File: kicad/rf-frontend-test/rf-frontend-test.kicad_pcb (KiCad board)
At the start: 2 copper layers, 15 x 26.4 mm, 26 parts, among them J1 GPIO, J2 SPI, J3 PWR, U1 Si4463, Y1 30MHz

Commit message: clean sch2
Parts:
- U1: footprint Package_DFN_QFN:QFN-20-1EP_4x4mm_P0.5mm_EP2.6x2.6mm_ThermalVias -> Package_DFN_QFN:QFN-20-1EP_4x4mm_P0.5mm_EP2.6x2.6mm
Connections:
- U1 pad 5: unconnected-(U1-NC-Pad5) -> GND
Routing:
- net GND: track 5.49 -> 13.1 mm, vias 75 -> 159
- net ~{RF_EN}: track 11.6 -> 12.5 mm
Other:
- board size 15 x 26.4 mm -> 15 x 26.5 mm

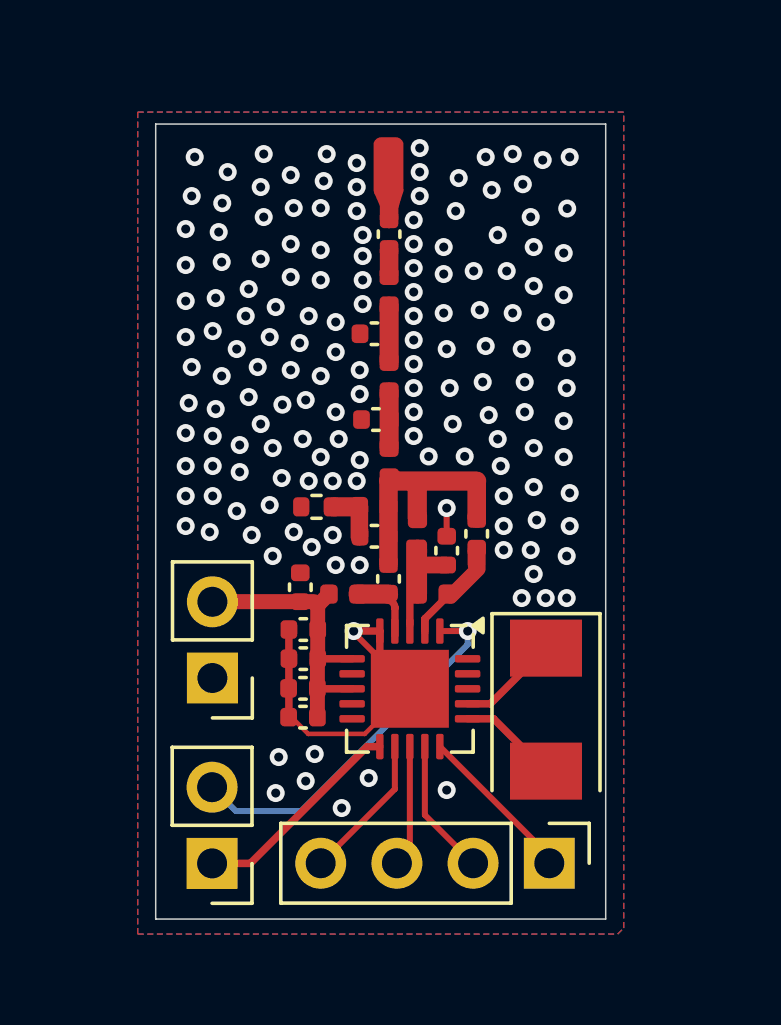
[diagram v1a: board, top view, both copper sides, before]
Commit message: Si4463 Transceiver Circuit V2.
Updated the transceiver board to make it compliant with EPL fab limitations. Fixed all GND vias, added Header Pins for the GPIO pins
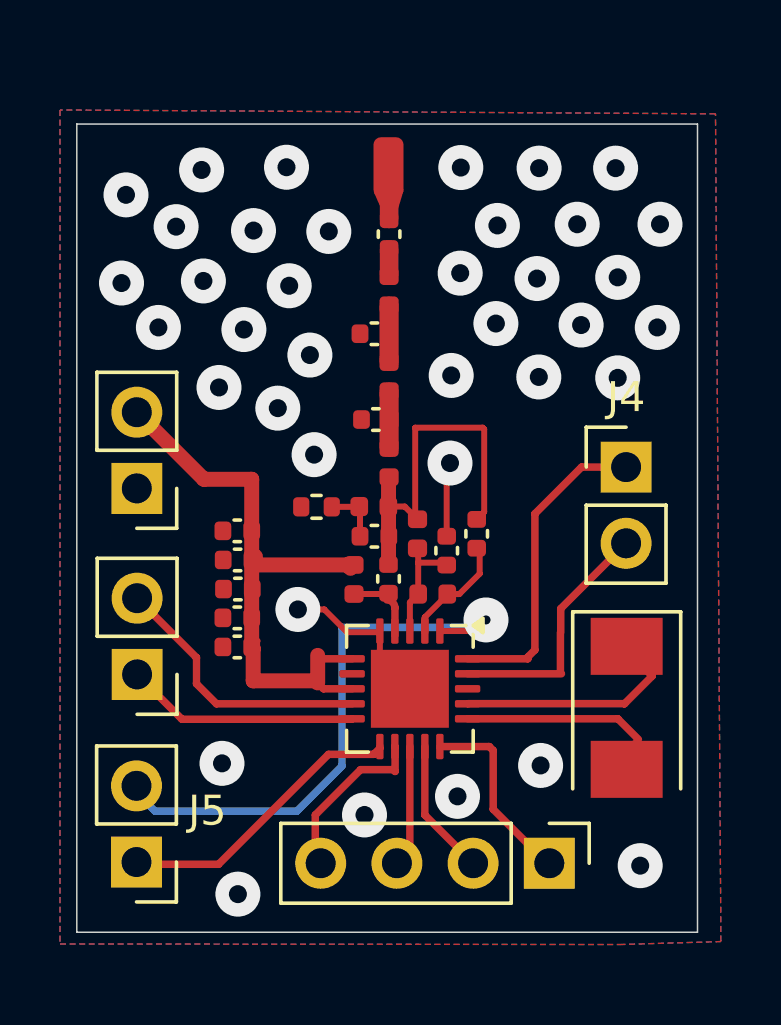
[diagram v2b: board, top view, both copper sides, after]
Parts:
- added J4: GPIO, Connector_PinHeader_2.54mm:PinHeader_1x02_P2.54mm_Vertical, F.Cu at (126.1, 57.2)
- added J5: GPIO, Connector_PinHeader_2.54mm:PinHeader_1x02_P2.54mm_Vertical, F.Cu at (109.8, 64.1)
- moved J3 6.80 mm to (109.8, 57.9)
- moved C4 3.21 mm to (113.1, 62.3)
- moved C1 3.20 mm to (113.1, 63.2)
- moved C2 3.19 mm to (113.1, 60.3)
- moved C5 3.18 mm to (113.1, 61.3)
- moved C3 2.82 mm to (113.1, 59.4), turned to 180 degrees
- moved Y1 2.69 mm to (126.1, 65.3)
- moved J1 2.52 mm to (109.8, 70.4)
- moved Lchk1 0.60 mm to (117.0, 61.0), turned to -90 degrees
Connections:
- U1 pad 10: unconnected-(U1-GPIO1-Pad10) -> GPIO1
- U1 pad 19: unconnected-(U1-GPIO2-Pad19) -> GPIO2
- U1 pad 20: unconnected-(U1-GPIO3-Pad20) -> GPIO3
- U1 pad 9: unconnected-(U1-GPIO0-Pad9) -> GPIO0
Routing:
- net Net-(C6-Pad2): track 0.00 -> 12.6 mm
- net +3.3V: track 10.1 -> 20.9 mm
- net GPIO3: track 0.00 -> 10.6 mm
- net GPIO0: track 0.00 -> 9.14 mm
- net GPIO2: track 0.00 -> 8.40 mm
- net GPIO1: track 0.00 -> 7.79 mm
- net ~{RF_EN}: track 12.5 -> 19.2 mm
- net GND: track 13.1 -> 8.04 mm, vias 159 -> 38
- net Net-(U1-XIN): track 3.38 -> 7.88 mm
- net Net-(U1-RXn): track 0.03 -> 3.90 mm
- net Net-(U1-XOUT): track 3.34 -> 7.14 mm
- net ~{RF_IRQ}: track 7.21 -> 9.92 mm
- net Net-(U1-RXp): track 1.51 -> 3.79 mm
- net Net-(CF1-Pad2): track 0.00 -> 1.92 mm
- net ~{RF_CS}: track 5.40 -> 6.68 mm
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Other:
- board size 15 x 26.5 mm -> 20.7 x 26.9 mm

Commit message: move some vias on rf frontend test board
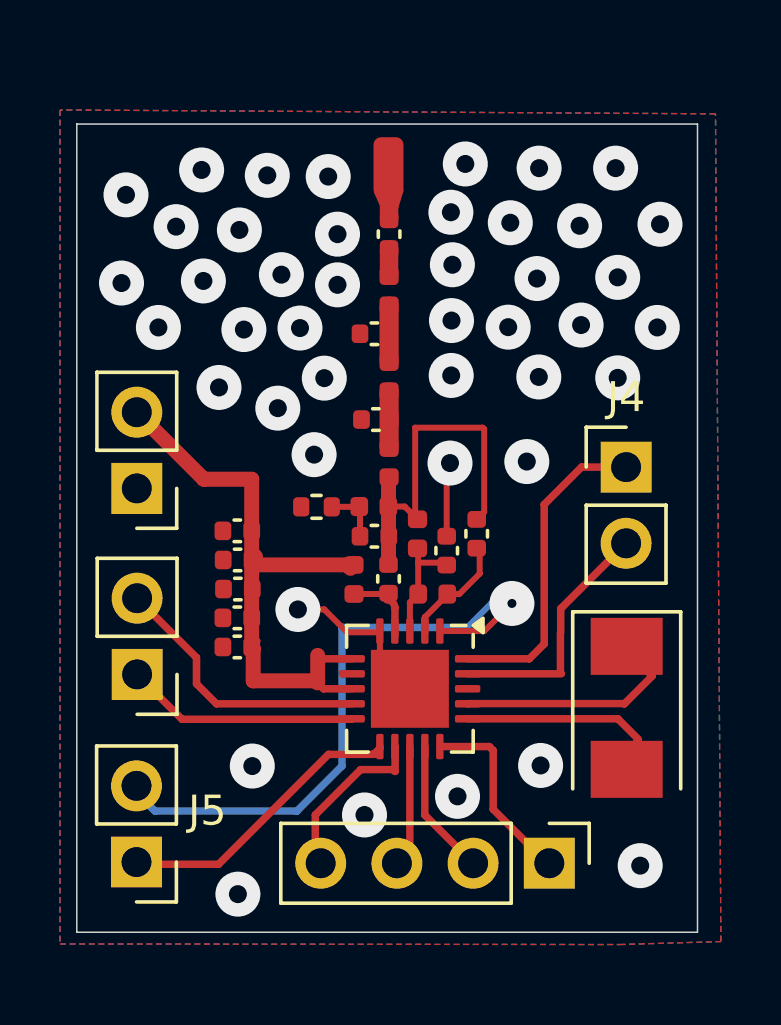
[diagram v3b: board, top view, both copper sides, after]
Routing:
- net ~{RF_EN}: track 19.2 -> 21.3 mm
- net GND: vias 38 -> 44
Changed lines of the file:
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@@
 	)
 	(segment
-		(start 119.872 62.7)
-		(end 121.04 62.7)
-		(width 0.2)
-		(layer "F.Cu")
-		(net 2)
-	)
-	(segment
-		(start 121.04 62.7)
-		(end 121.41 62.33)
-		(width 0.2)
-		(layer "F.Cu")
-		(net 2)
-	)
-	(via
-		(at 121.41 62.33)
+		(start 121.355 62.7)
+		(end 119.872 62.7)
+		(width 0.2)
+		(layer "F.Cu")
+		(net 2)
+	)
+	(segment
+		(start 122.275 61.78)
+		(end 121.355 62.7)
+		(width 0.2)
+		(layer "F.Cu")
+		(net 2)
+	)
+	(via
+		(at 122.275 61.78)
 		(size 1.5)
 		(drill 0.3)
@@
 	)
 	(segment
-		(start 121.03 62.33)
+		(start 121.58 61.78)
 		(end 120.78 62.58)
 		(width 0.2)
@@
 	)
 	(segment
-		(start 121.41 62.33)
-		(end 121.03 62.33)
+		(start 122.275 61.78)
+		(end 121.58 61.78)
 		(width 0.2)
 		(layer "B.Cu")
@@
 	)
 	(segment
-		(start 123.04 63.33)
-		(end 123.04 58.79)
-		(width 0.25)
-		(layer "F.Cu")
-		(net 7)
-	)
-	(segment
-		(start 122.805 63.625)
-		(end 122.805 63.565)
-		(width 0.25)
-		(layer "F.Cu")
-		(net 7)
-	)
-	(segment
-		(start 120.797 63.625)
-		(end 122.805 63.625)
-		(width 0.25)
-		(layer "F.Cu")
-		(net 7)
-	)
-	(segment
-		(start 123.04 58.79)
-		(end 124.595 57.235)
-		(width 0.25)
-		(layer "F.Cu")
-		(net 7)
-	)
-	(segment
-		(start 122.805 63.565)
-		(end 123.04 63.33)
+		(start 122.855 63.625)
+		(end 123.35 63.13)
 		(width 0.25)
 		(layer "F.Cu")
@@
 	)
 	(segment
+		(start 123.35 63.13)
+		(end 123.35 58.48)
+		(width 0.25)
+		(layer "F.Cu")
+		(net 7)
+	)
+	(segment
+		(start 123.35 58.48)
+		(end 124.595 57.235)
+		(width 0.25)
+		(layer "F.Cu")
+		(net 7)
+	)
+	(segment
+		(start 120.797 63.625)
+		(end 122.855 63.625)
+		(width 0.25)
+		(layer "F.Cu")
+		(net 7)
+	)
+	(segment
 		(start 112.425 65.125)
 		(end 111.76 64.46)
@@
 	)
 	(via
-		(at 120.57 47.25)
-		(size 1.5)
-		(drill 0.6)
-		(layers "F.Cu" "B.Cu")
-		(net 20)
-	)
-	(via
-		(at 124.45 49.14)
+		(at 120.72 47.13)
+		(size 1.5)
+		(drill 0.6)
+		(layers "F.Cu" "B.Cu")
+		(net 20)
+	)
+	(via
+		(at 124.53 49.19)
 		(size 1.5)
 		(drill 0.6)
@@
 	)
 	(via
-		(at 115.54 53.5)
+		(at 114.59 50.82)
+		(size 1.5)
+		(drill 0.6)
+		(layers "F.Cu" "B.Cu")
+		(net 20)
+	)
+	(via
+		(at 116.02 54.27)
 		(size 1.5)
 		(drill 0.6)
@@
 	)
 	(via
-		(at 116.17 49.38)
-		(size 1.5)
-		(drill 0.6)
-		(layers "F.Cu" "B.Cu")
-		(net 20)
-	)
-	(via
-		(at 114.76 47.24)
+		(at 115.21 52.6)
+		(size 1.5)
+		(drill 0.6)
+		(layers "F.Cu" "B.Cu")
+		(net 20)
+	)
+	(via
+		(at 116.46 49.47)
+		(size 1.5)
+		(drill 0.6)
+		(layers "F.Cu" "B.Cu")
+		(net 20)
+	)
+	(via
+		(at 116.15 47.55)
 		(size 1.5)
 		(drill 0.6)
@@
 	)
 	(via
+		(at 113.19 49.33)
+		(size 1.5)
+		(drill 0.6)
+		(layers "F.Cu" "B.Cu")
+		(net 20)
+	)
+	(via
 		(at 120.46 68.21)
 		(size 1.5)
@@
 	)
 	(via
-		(at 121.79 49.18)
+		(at 122.22 49.09)
+		(size 1.5)
+		(drill 0.6)
+		(layers "F.Cu" "B.Cu")
+		(net 20)
+	)
+	(via
+		(at 120.24 48.74)
 		(size 1.5)
 		(drill 0.6)
@@
 	)
 	(via
-		(at 113.66 49.35)
+		(at 114.12 47.51)
+		(size 1.5)
+		(drill 0.6)
+		(layers "F.Cu" "B.Cu")
+		(net 20)
+	)
+	(via
+		(at 122.15 52.57)
 		(size 1.5)
 		(drill 0.6)
@@
 	)
 	(via
+		(at 122.77 57.05)
+		(size 1.5)
+		(drill 0.6)
+		(layers "F.Cu" "B.Cu")
+		(net 20)
+	)
+	(via
 		(at 123.23 67.18)
 		(size 1.5)
@@
 	)
 	(via
-		(at 112.61 67.11)
+		(at 113.62 67.2)
 		(size 1.5)
 		(drill 0.6)
@@
 	)
 	(via
-		(at 120.55 50.77)
+		(at 120.29 50.49)
 		(size 1.5)
 		(drill 0.6)
@@
 	)
 	(via
-		(at 121.74 52.45)
-		(size 1.5)
-		(drill 0.6)
-		(layers "F.Cu" "B.Cu")
-		(net 20)
-	)
-	(via
-		(at 114.85 51.19)
-		(size 1.5)
-		(drill 0.6)
+		(at 120.26 52.35)
+		(size 1.5)
+		(drill 0.6)
+		(layers "F.Cu" "B.Cu")
+		(net 20)
+	)
+	(via
+		(at 116.46 51.16)
+		(size 1.5)
+		(drill 0.6)

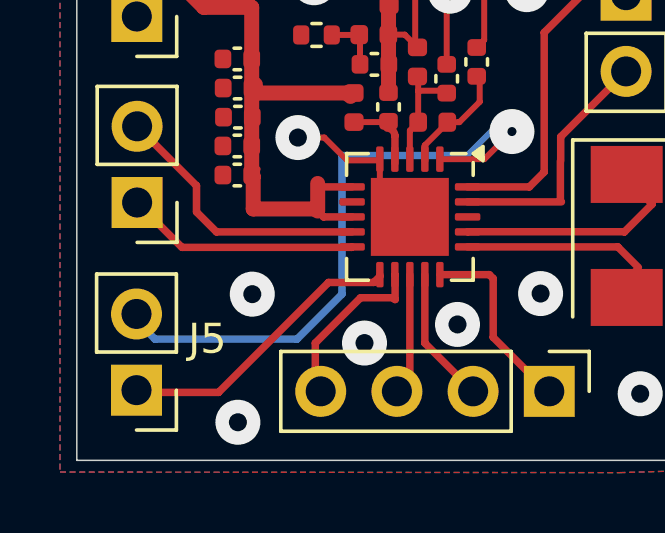
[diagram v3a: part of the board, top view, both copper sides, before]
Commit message: reroute rf_en on rf frontend test for assembly ease
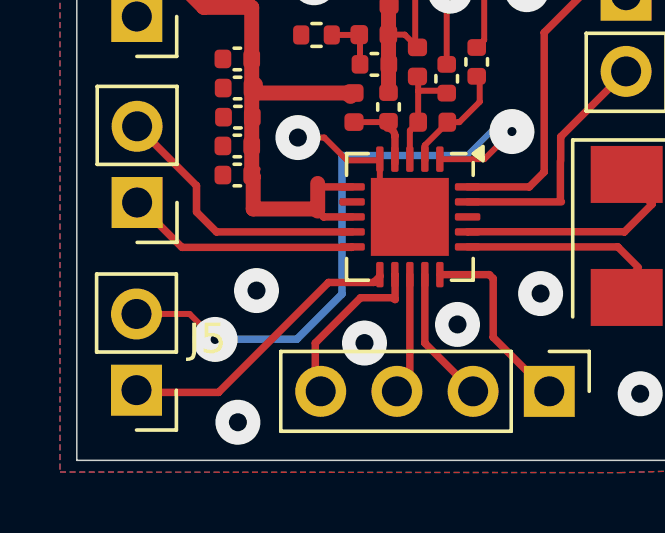
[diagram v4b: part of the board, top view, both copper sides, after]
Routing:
- net ~{RF_EN}: track 21.3 -> 21.2 mm, vias 1 -> 2
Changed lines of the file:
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@@
+	)
+	(segment
+		(start 111.53 67.86)
+		(end 112.38 68.71)
+		(width 0.2)
+		(layer "F.Cu")
+		(net 2)
+	)
+	(segment
+		(start 109.76 67.86)
+		(end 111.53 67.86)
+		(width 0.2)
+		(layer "F.Cu")
+		(net 2)
 	)
 	(segment
@@
 	)
 	(via
+		(at 112.38 68.71)
+		(size 1.5)
+		(drill 0.3)
+		(layers "F.Cu" "B.Cu")
+		(net 2)
+	)
+	(via
 		(at 122.275 61.78)
 		(size 1.5)
@@
 	)
 	(segment
-		(start 110.375 68.7)
-		(end 109.61 67.935)
-		(width 0.25)
-		(layer "B.Cu")
-		(net 2)
-	)
-	(segment
 		(start 115.11 68.7)
 		(end 116.61 67.2)
@@
 	)
 	(segment
-		(start 115.11 68.7)
-		(end 110.375 68.7)
+		(start 112.39 68.7)
+		(end 112.38 68.71)
 		(width 0.25)
 		(layer "B.Cu")
@@
 	)
 	(segment
+		(start 115.11 68.7)
+		(end 112.39 68.7)
+		(width 0.25)
+		(layer "B.Cu")
+		(net 2)
+	)
+	(segment
 		(start 116.61 67.2)
 		(end 116.61 62.58)
@@
 	)
 	(via
-		(at 113.62 67.2)
-		(size 1.5)
-		(drill 0.6)
+		(at 113.76 67.08)
+		(size 1.5)
+		(drill 0.6)

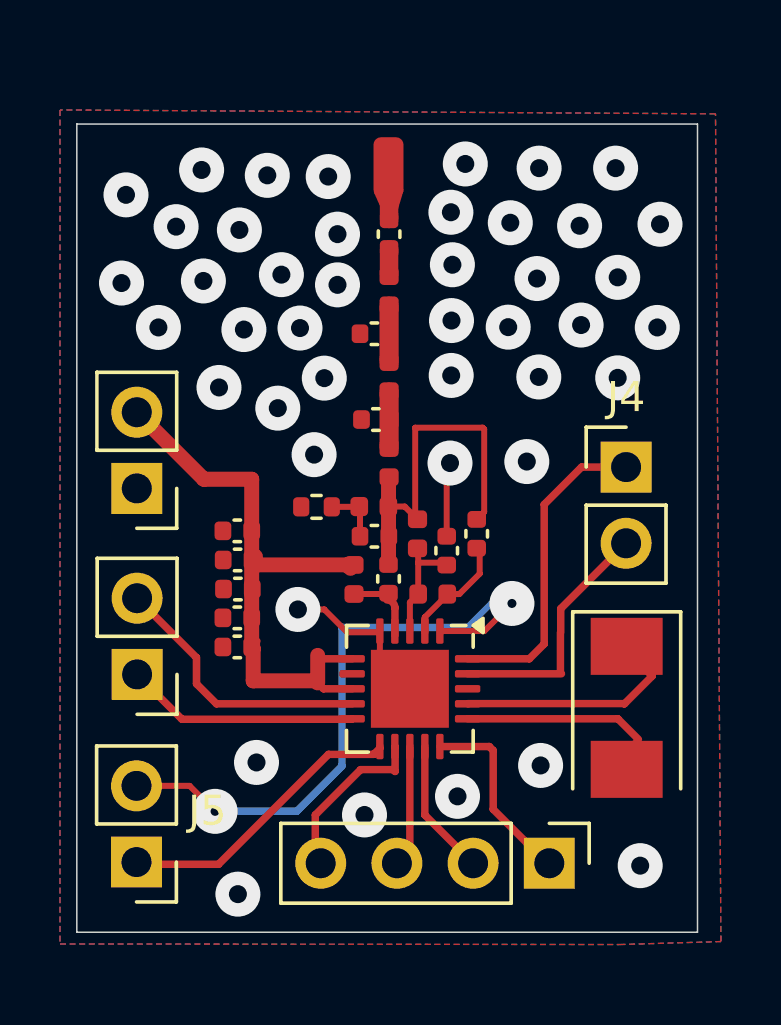
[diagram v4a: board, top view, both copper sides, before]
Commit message: slight value changes to rf frontend
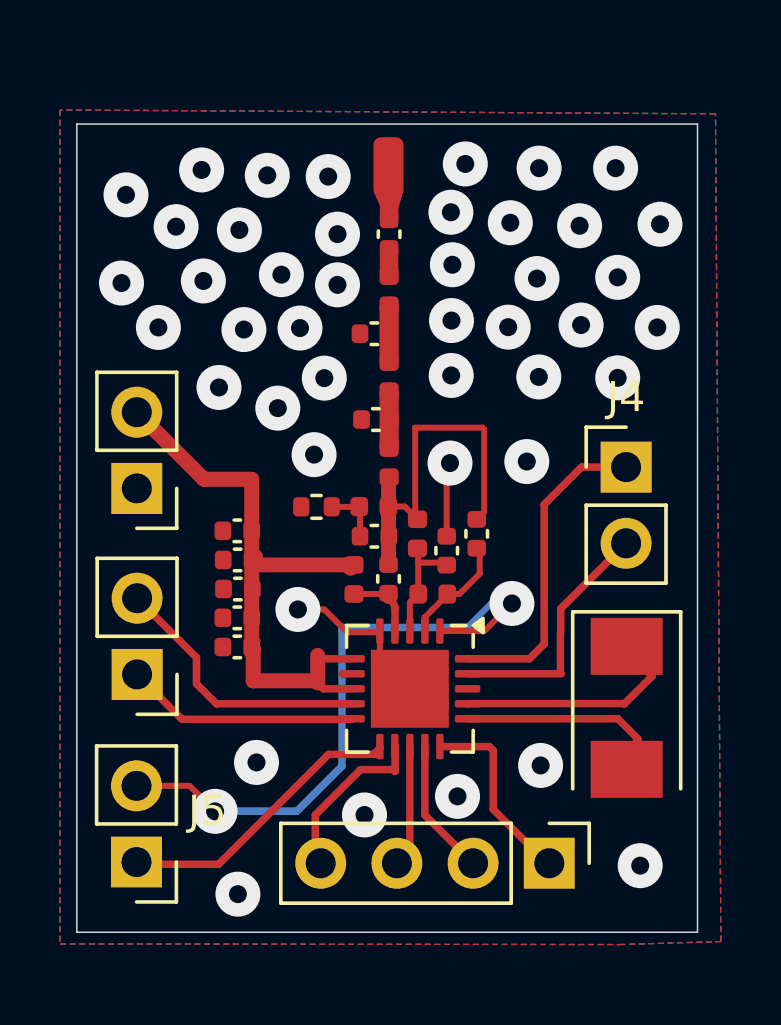
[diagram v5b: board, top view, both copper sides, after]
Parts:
- CF1: value 36p -> 30p
- CR1: value 14p -> 13p
- LF1: value 33n -> 39n
- LR2: value 180n -> 150n
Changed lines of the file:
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@@
 			)
 		)
-		(property "Value" "14p"
+		(property "Value" "13p"
 			(at 0 1.16 90)
 			(layer "F.Fab")
@@
 			)
 		)
-		(property "Value" "36p"
+		(property "Value" "30p"
 			(at 0 1.16 0)
 			(layer "F.Fab")
@@
 			)
 		)
-		(property "Value" "180n"
+		(property "Value" "150n"
 			(at 0 1.17 90)
 			(layer "F.Fab")
@@
 			)
 		)
-		(property "Value" "33n"
+		(property "Value" "39n"
 			(at 0 1.17 0)
 			(layer "F.Fab")
@@
 		(at 112.38 68.71)
 		(size 1.5)
-		(drill 0.3)
+		(drill 0.6)
 		(layers "F.Cu" "B.Cu")
 		(net 2)
@@
 		(at 122.275 61.78)
 		(size 1.5)
-		(drill 0.3)
+		(drill 0.6)
 		(layers "F.Cu" "B.Cu")
 		(net 2)
